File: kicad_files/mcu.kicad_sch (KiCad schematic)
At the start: 0 parts

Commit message: commit
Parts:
- added .1: DFRobot RP2350 Module, symbol custom_symbols:rp2350_beetle_module
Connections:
- new net 3.3_Volts: .1.3V3 (3.3_Volts)
- new net 5_Volts: .1.Vcc (5_Volts)
- new net Battery_Charge: .1.BAT (Battery_Charge)
- new net Ground: .1.GND (Ground)
- new net batteryLevClkPin: .1.5 (batteryLevClkPin)
- new net batteryLevDataPin: .1.4 (batteryLevDataPin)
- new net batteryLevTrigPin: .1.1 (batteryLevTrigPin)
- new net larvDumpMotor: .1.27 (larvDumpMotor)
- new net larvLevelSonarEcho: .1.18 (larvLevelSonarEcho)
- new net larvLevelSonarTrig: .1.16 (larvLevelSonarTrig)
- new net uiServo: .1.19 (uiServo)
- new net washoutIn: .1.26 (washoutIn)
- new net washoutSonarEcho: .1.9 (washoutSonarEcho)
- new net washoutSonarTrig: .1.8 (washoutSonarTrig)

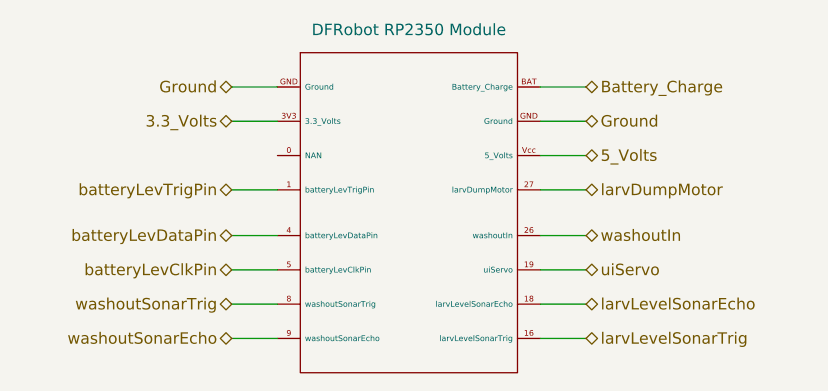
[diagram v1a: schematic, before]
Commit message: Initial power system implementation
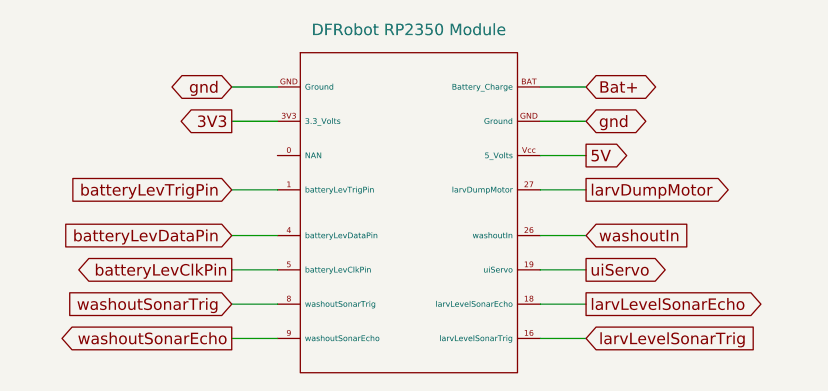
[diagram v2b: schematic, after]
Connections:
- net 3.3_Volts renamed 3V3
- net 5_Volts renamed 5V
- net Battery_Charge renamed Bat+
- net Ground renamed gnd
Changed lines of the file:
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@@
 		)
 	)
-	(hierarchical_label "batteryLevTrigPin"
-		(shape bidirectional)
+	(global_label "batteryLevTrigPin"
+		(shape input)
 		(at 129.54 97.79 180)
-		(effects
-			(font
-				(size 1.27 1.27)
-			)
-			(justify right)
-		)
-	)
-	(hierarchical_label "washoutIn"
-		(shape bidirectional)
-		(at 168.91 102.87 0)
-		(effects
-			(font
-				(size 1.27 1.27)
-			)
-			(justify left)
-		)
-	)
-	(hierarchical_label "5_Volts"
-		(shape bidirectional)
-		(at 168.91 93.98 0)
-		(effects
-			(font
-				(size 1.27 1.27)
-			)
-			(justify left)
-		)
-	)
-	(hierarchical_label "larvDumpMotor"
-		(shape bidirectional)
-		(at 168.91 97.79 0)
-		(effects
-			(font
-				(size 1.27 1.27)
-			)
-			(justify left)
-		)
-	)
-	(hierarchical_label "Ground"
+		(fields_autoplaced yes)
+		(effects
+			(font
+				(size 1.27 1.27)
+			)
+			(justify right)
+		)
+		(property "Intersheetrefs" "${INTERSHEET_REFS}"
+			(at 110.3473 97.79 0)
+			(effects
+				(font
+					(size 1.27 1.27)
+				)
+				(justify right)
+				(hide yes)
+			)
+		)
+	)
+	(global_label "gnd"
 		(shape bidirectional)
 		(at 129.54 86.36 180)
-		(effects
-			(font
-				(size 1.27 1.27)
-			)
-			(justify right)
-		)
-	)
-	(hierarchical_label "washoutSonarEcho"
+		(fields_autoplaced yes)
+		(effects
+			(font
+				(size 1.27 1.27)
+			)
+			(justify right)
+		)
+		(property "Intersheetrefs" "${INTERSHEET_REFS}"
+			(at 121.9965 86.36 0)
+			(effects
+				(font
+					(size 1.27 1.27)
+				)
+				(justify right)
+				(hide yes)
+			)
+		)
+	)
+	(global_label "larvLevelSonarEcho"
+		(shape output)
+		(at 168.91 110.49 0)
+		(fields_autoplaced yes)
+		(effects
+			(font
+				(size 1.27 1.27)
+			)
+			(justify left)
+		)
+		(property "Intersheetrefs" "${INTERSHEET_REFS}"
+			(at 190.2796 110.49 0)
+			(effects
+				(font
+					(size 1.27 1.27)
+				)
+				(justify left)
+				(hide yes)
+			)
+		)
+	)
+	(global_label "gnd"
 		(shape bidirectional)
-		(at 129.54 114.3 180)
-		(effects
-			(font
-				(size 1.27 1.27)
-			)
-			(justify right)
-		)
-	)
-	(hierarchical_label "washoutSonarTrig"
-		(shape bidirectional)
-		(at 129.54 110.49 180)
-		(effects
-			(font
-				(size 1.27 1.27)
-			)
-			(justify right)
-		)
-	)
-	(hierarchical_label "3.3_Volts"
-		(shape bidirectional)
+		(at 168.91 90.17 0)
+		(fields_autoplaced yes)
+		(effects
+			(font
+				(size 1.27 1.27)
+			)
+			(justify left)
+		)
+		(property "Intersheetrefs" "${INTERSHEET_REFS}"
+			(at 176.4535 90.17 0)
+			(effects
+				(font
+					(size 1.27 1.27)
+				)
+				(justify left)
+				(hide yes)
+			)
+		)
+	)
+	(global_label "batteryLevDataPin"
+		(shape input)
+		(at 129.54 102.87 180)
+		(fields_autoplaced yes)
+		(effects
+			(font
+				(size 1.27 1.27)
+			)
+			(justify right)
+		)
+		(property "Intersheetrefs" "${INTERSHEET_REFS}"
+			(at 109.5612 102.87 0)
+			(effects
+				(font
+					(size 1.27 1.27)
+				)
+				(justify right)
+				(hide yes)
+			)
+		)
+	)
+	(global_label "3V3"
+		(shape output)
 		(at 129.54 90.17 180)
-		(effects
-			(font
-				(size 1.27 1.27)
-			)
-			(justify right)
-		)
-	)
-	(hierarchical_label "Battery_Charge"
+		(fields_autoplaced yes)
+		(effects
+			(font
+				(size 1.27 1.27)
+			)
+			(justify right)
+		)
+		(property "Intersheetrefs" "${INTERSHEET_REFS}"
+			(at 123.0472 90.17 0)
+			(effects
+				(font
+					(size 1.27 1.27)
+				)
+				(justify right)
+				(hide yes)
+			)
+		)
+	)
+	(global_label "larvLevelSonarTrig"
+		(shape input)
+		(at 168.91 114.3 0)
+		(fields_autoplaced yes)
+		(effects
+			(font
+				(size 1.27 1.27)
+			)
+			(justify left)
+		)
+		(property "Intersheetrefs" "${INTERSHEET_REFS}"
+			(at 189.2516 114.3 0)
+			(effects
+				(font
+					(size 1.27 1.27)
+				)
+				(justify left)
+				(hide yes)
+			)
+		)
+	)
+	(global_label "larvDumpMotor"
+		(shape output)
+		(at 168.91 97.79 0)
+		(fields_autoplaced yes)
+		(effects
+			(font
+				(size 1.27 1.27)
+			)
+			(justify left)
+		)
+		(property "Intersheetrefs" "${INTERSHEET_REFS}"
+			(at 185.9858 97.79 0)
+			(effects
+				(font
+					(size 1.27 1.27)
+				)
+				(justify left)
+				(hide yes)
+			)
+		)
+	)
+	(global_label "Bat+"
 		(shape bidirectional)
 		(at 168.91 86.36 0)
-		(effects
-			(font
-				(size 1.27 1.27)
-			)
-			(justify left)
-		)
-	)
-	(hierarchical_label "larvLevelSonarTrig"
-		(shape bidirectional)
-		(at 168.91 114.3 0)
-		(effects
-			(font
-				(size 1.27 1.27)
-			)
-			(justify left)
-		)
-	)
-	(hierarchical_label "batteryLevDataPin"
-		(shape bidirectional)
-		(at 129.54 102.87 180)
-		(effects
-			(font
-				(size 1.27 1.27)
-			)
-			(justify right)
-		)
-	)
-	(hierarchical_label "batteryLevClkPin"
-		(shape bidirectional)
+		(fields_autoplaced yes)
+		(effects
+			(font
+				(size 1.27 1.27)
+			)
+			(justify left)
+		)
+		(property "Intersheetrefs" "${INTERSHEET_REFS}"
+			(at 177.7236 86.36 0)
+			(effects
+				(font
+					(size 1.27 1.27)
+				)
+				(justify left)
+				(hide yes)
+			)
+		)
+	)
+	(global_label "washoutSonarTrig"
+		(shape input)
+		(at 129.54 110.49 180)
+		(fields_autoplaced yes)
+		(effects
+			(font
+				(size 1.27 1.27)
+			)
+			(justify right)
+		)
+		(property "Intersheetrefs" "${INTERSHEET_REFS}"
+			(at 109.9242 110.49 0)
+			(effects
+				(font
+					(size 1.27 1.27)
+				)
+				(justify right)
+				(hide yes)
+			)
+		)
+	)
+	(global_label "batteryLevClkPin"
+		(shape output)
 		(at 129.54 106.68 180)
-		(effects
-			(font
-				(size 1.27 1.27)
-			)
-			(justify right)
-		)
-	)
-	(hierarchical_label "Ground"
-		(shape bidirectional)
-		(at 168.91 90.17 0)
-		(effects
-			(font
-				(size 1.27 1.27)
-			)
-			(justify left)
-		)
-	)
-	(hierarchical_label "uiServo"
-		(shape bidirectional)
+		(fields_autoplaced yes)
+		(effects
+			(font
+				(size 1.27 1.27)
+			)
+			(justify right)
+		)
+		(property "Intersheetrefs" "${INTERSHEET_REFS}"
+			(at 110.8916 106.68 0)
+			(effects
+				(font
+					(size 1.27 1.27)
+				)
+				(justify right)
+				(hide yes)
+			)
+		)
+	)
+	(global_label "uiServo"
+		(shape output)
 		(at 168.91 106.68 0)
-		(effects
-			(font
-				(size 1.27 1.27)
-			)
-			(justify left)
-		)
-	)
-	(hierarchical_label "larvLevelSonarEcho"
-		(shape bidirectional)
-		(at 168.91 110.49 0)
-		(effects
-			(font
-				(size 1.27 1.27)
-			)
-			(justify left)
-		)
-	)
+		(fields_autoplaced yes)
+		(effects
+			(font
+				(size 1.27 1.27)
+			)
+			(justify left)
+		)
+		(property "Intersheetrefs" "${INTERSHEET_REFS}"
+			(at 178.8499 106.68 0)
+			(effects
+				(font
+					(size 1.27 1.27)
+				)
+				(justify left)
+				(hide yes)
+			)
+		)
+	)
+	(global_label "5V"
+		(shape output)
+		(at 168.91 93.98 0)
+		(fields_autoplaced yes)
+		(effects
+			(font
+				(size 1.27 1.27)
+			)
+			(justify left)
+		)
+		(property "Intersheetrefs" "${INTERSHEET_REFS}"
+			(at 174.1933 93.98 0)
+			(effects
+				(font
+					(size 1.27 1.27)
+				)
+				(justify left)
+				(hide yes)
+			)
+		)
+	)
+	(global_label "washoutIn"
+		(shape input)
+		(at 168.91 102.87 0)
+		(fields_autoplaced yes)
+		(effects
+			(font
+				(size 1.27 1.27)
+			)
+			(justify left)
+		)
+		(property "Intersheetrefs" "${INTERSHEET_REFS}"
+			(at 181.3293 102.87 0)
+			(effects
+				(font
+					(size 1.27 1.27)
+				)
+				(justify left)
+				(hide yes)
+			)
+		)
+	)
+	(global_label "washoutSonarEcho"
+		(shape output)
+		(at 129.54 114.3 180)
+		(fields_autoplaced yes)
+		(effects
+			(font
+				(size 1.27 1.27)
+			)
+			(justify right)
+		)
+		(property "Intersheetrefs" "${INTERSHEET_REFS}"
+			(at 108.8962 114.3 0)
+			(effects
+				(font
+					(size 1.27 1.27)
+				)
+				(justify right)
+				(hide yes)
+			)
+		)
+	)

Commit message: Hierarchical labels finished. Flyback diode issue fixed. I2C pins added
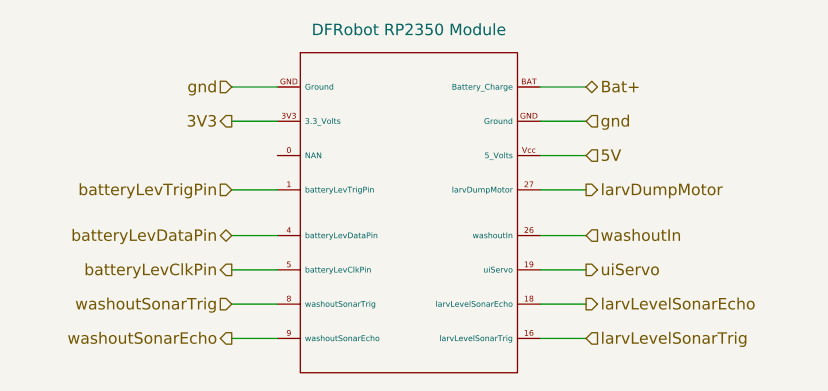
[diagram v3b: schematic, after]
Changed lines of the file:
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@@
 		)
 	)
-	(global_label "batteryLevTrigPin"
+	(hierarchical_label "washoutIn"
 		(shape input)
-		(at 129.54 97.79 180)
-		(fields_autoplaced yes)
+		(at 168.91 102.87 0)
+		(effects
+			(font
+				(size 1.27 1.27)
+			)
+			(justify left)
+		)
+	)
+	(hierarchical_label "washoutSonarTrig"
+		(shape input)
+		(at 129.54 110.49 180)
 		(effects
 			(font
@@
 			(justify right)
 		)
-		(property "Intersheetrefs" "${INTERSHEET_REFS}"
-			(at 110.3473 97.79 0)
-			(effects
-				(font
-					(size 1.27 1.27)
-				)
-				(justify right)
-				(hide yes)
+	)
+	(hierarchical_label "larvDumpMotor"
+		(shape output)
+		(at 168.91 97.79 0)
+		(effects
+			(font
+				(size 1.27 1.27)
 			)
+			(justify left)
 		)
 	)
-	(global_label "gnd"
-		(shape bidirectional)
-		(at 129.54 86.36 180)
-		(fields_autoplaced yes)
+	(hierarchical_label "batteryLevClkPin"
+		(shape output)
+		(at 129.54 106.68 180)
 		(effects
 			(font
@@
 			(justify right)
 		)
-		(property "Intersheetrefs" "${INTERSHEET_REFS}"
-			(at 121.9965 86.36 0)
-			(effects
-				(font
-					(size 1.27 1.27)
-				)
-				(justify right)
-				(hide yes)
-			)
-		)
 	)
-	(global_label "larvLevelSonarEcho"
-		(shape output)
-		(at 168.91 110.49 0)
-		(fields_autoplaced yes)
+	(hierarchical_label "Bat+"
+		(shape bidirectional)
+		(at 168.91 86.36 0)
 		(effects
 			(font
@@
 			(justify left)
 		)
-		(property "Intersheetrefs" "${INTERSHEET_REFS}"
-			(at 190.2796 110.49 0)
-			(effects
-				(font
-					(size 1.27 1.27)
-				)
-				(justify left)
-				(hide yes)
-			)
-		)
 	)
-	(global_label "gnd"
-		(shape bidirectional)
+	(hierarchical_label "gnd"
+		(shape input)
 		(at 168.91 90.17 0)
-		(fields_autoplaced yes)
 		(effects
 			(font
@@
 			(justify left)
 		)
-		(property "Intersheetrefs" "${INTERSHEET_REFS}"
-			(at 176.4535 90.17 0)
-			(effects
-				(font
-					(size 1.27 1.27)
-				)
-				(justify left)
-				(hide yes)
-			)
-		)
 	)
-	(global_label "batteryLevDataPin"
+	(hierarchical_label "gnd"
 		(shape input)
-		(at 129.54 102.87 180)
-		(fields_autoplaced yes)
+		(at 129.54 86.36 180)
 		(effects
 			(font
@@
 			(justify right)
 		)
-		(property "Intersheetrefs" "${INTERSHEET_REFS}"
-			(at 109.5612 102.87 0)
-			(effects
-				(font
-					(size 1.27 1.27)
-				)
-				(justify right)
-				(hide yes)
+	)
+	(hierarchical_label "larvLevelSonarTrig"
+		(shape input)
+		(at 168.91 114.3 0)
+		(effects
+			(font
+				(size 1.27 1.27)
 			)
+			(justify left)
 		)
 	)
-	(global_label "3V3"
+	(hierarchical_label "washoutSonarEcho"
 		(shape output)
-		(at 129.54 90.17 180)
-		(fields_autoplaced yes)
+		(at 129.54 114.3 180)
 		(effects
 			(font
@@
 			(justify right)
 		)
-		(property "Intersheetrefs" "${INTERSHEET_REFS}"
-			(at 123.0472 90.17 0)
-			(effects
-				(font
-					(size 1.27 1.27)
-				)
-				(justify right)
-				(hide yes)
+	)
+	(hierarchical_label "3V3"
+		(shape output)
+		(at 129.54 90.17 180)
+		(effects
+			(font
+				(size 1.27 1.27)
 			)
+			(justify right)
 		)
 	)
-	(global_label "larvLevelSonarTrig"
+	(hierarchical_label "batteryLevTrigPin"
 		(shape input)
-		(at 168.91 114.3 0)
-		(fields_autoplaced yes)
+		(at 129.54 97.79 180)
+		(effects
+			(font
+				(size 1.27 1.27)
+			)
+			(justify right)
+		)
+	)
+	(hierarchical_label "uiServo"
+		(shape output)
+		(at 168.91 106.68 0)
 		(effects
 			(font
@@
 			(justify left)
 		)
-		(property "Intersheetrefs" "${INTERSHEET_REFS}"
-			(at 189.2516 114.3 0)
-			(effects
-				(font
-					(size 1.27 1.27)
-				)
-				(justify left)
-				(hide yes)
-			)
-		)
 	)
-	(global_label "larvDumpMotor"
+	(hierarchical_label "larvLevelSonarEcho"
 		(shape output)
-		(at 168.91 97.79 0)
-		(fields_autoplaced yes)
+		(at 168.91 110.49 0)
 		(effects
 			(font
@@
 			(justify left)
 		)
-		(property "Intersheetrefs" "${INTERSHEET_REFS}"
-			(at 185.9858 97.79 0)
-			(effects
-				(font
-					(size 1.27 1.27)
-				)
-				(justify left)
-				(hide yes)
-			)
-		)
 	)
-	(global_label "Bat+"
-		(shape bidirectional)
-		(at 168.91 86.36 0)
-		(fields_autoplaced yes)
+	(hierarchical_label "5V"
+		(shape input)
+		(at 168.91 93.98 0)
 		(effects
 			(font
@@
 			(justify left)
 		)
-		(property "Intersheetrefs" "${INTERSHEET_REFS}"
-			(at 177.7236 86.36 0)
-			(effects
-				(font
-					(size 1.27 1.27)
-				)
-				(justify left)
-				(hide yes)
-			)
-		)
 	)
-	(global_label "washoutSonarTrig"
-		(shape input)
-		(at 129.54 110.49 180)
-		(fields_autoplaced yes)
+	(hierarchical_label "batteryLevDataPin"
+		(shape bidirectional)
+		(at 129.54 102.87 180)
 		(effects
 			(font
@@
 			(justify right)
 		)
-		(property "Intersheetrefs" "${INTERSHEET_REFS}"
-			(at 109.9242 110.49 0)
-			(effects
-				(font
-					(size 1.27 1.27)
-				)
-				(justify right)
-				(hide yes)
-			)
-		)
 	)
-	(global_label "batteryLevClkPin"
-		(shape output)
-		(at 129.54 106.68 180)
-		(fields_autoplaced yes)
-		(effects
-			(font
-				(size 1.27 1.27)
-			)
-			(justify right)
-		)
-		(property "Intersheetrefs" "${INTERSHEET_REFS}"
-			(at 110.8916 106.68 0)
-			(effects
-				(font
-					(size 1.27 1.27)
-				)
-				(justify right)
-				(hide yes)
-			)
-		)
-	)
-	(global_label "uiServo"
-		(shape output)
-		(at 168.91 106.68 0)
-		(fields_autoplaced yes)
-		(effects
-			(font
-				(size 1.27 1.27)
-			)
-			(justify left)
-		)
-		(property "Intersheetrefs" "${INTERSHEET_REFS}"
-			(at 178.8499 106.68 0)
-			(effects
-				(font
-					(size 1.27 1.27)
-				)
-				(justify left)
-				(hide yes)
-			)
-		)
-	)
-	(global_label "5V"
-		(shape output)
-		(at 168.91 93.98 0)
-		(fields_autoplaced yes)
-		(effects
-			(font
-				(size 1.27 1.27)
-			)
-			(justify left)
-		)
-		(property "Intersheetrefs" "${INTERSHEET_REFS}"
-			(at 174.1933 93.98 0)
-			(effects
-				(font
-					(size 1.27 1.27)
-				)
-				(justify left)
-				(hide yes)
-			)
-		)
-	)
-	(global_label "washoutIn"
-		(shape input)
-		(at 168.91 102.87 0)
-		(fields_autoplaced yes)
-		(effects
-			(font
-				(size 1.27 1.27)
-			)
-			(justify left)
-		)
-		(property "Intersheetrefs" "${INTERSHEET_REFS}"
-			(at 181.3293 102.87 0)
-			(effects
-				(font
-					(size 1.27 1.27)
-				)
-				(justify left)
-				(hide yes)
-			)
-		)
-	)
-	(global_label "washoutSonarEcho"
-		(shape output)
-		(at 129.54 114.3 180)
-		(fields_autoplaced yes)
-		(effects
-			(font
-				(size 1.27 1.27)
-			)
-			(justify right)
-		)
-		(property "Intersheetrefs" "${INTERSHEET_REFS}"
-			(at 108.8962 114.3 0)
-			(effects
-				(font
-					(size 1.27 1.27)
-				)
-				(justify right)
-				(hide yes)
-			)
-		)
-	)

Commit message: Partial footprint assignment
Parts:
- .1: footprint (none) -> rp2350_footprint:DFR1188-DIP
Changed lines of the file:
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@@
 			)
 		)
-		(property "Footprint" ""
+		(property "Footprint" "rp2350_footprint:DFR1188-DIP"
 			(at 137.16 82.55 0)
 			(effects
